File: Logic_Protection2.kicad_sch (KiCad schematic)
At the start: 10 parts

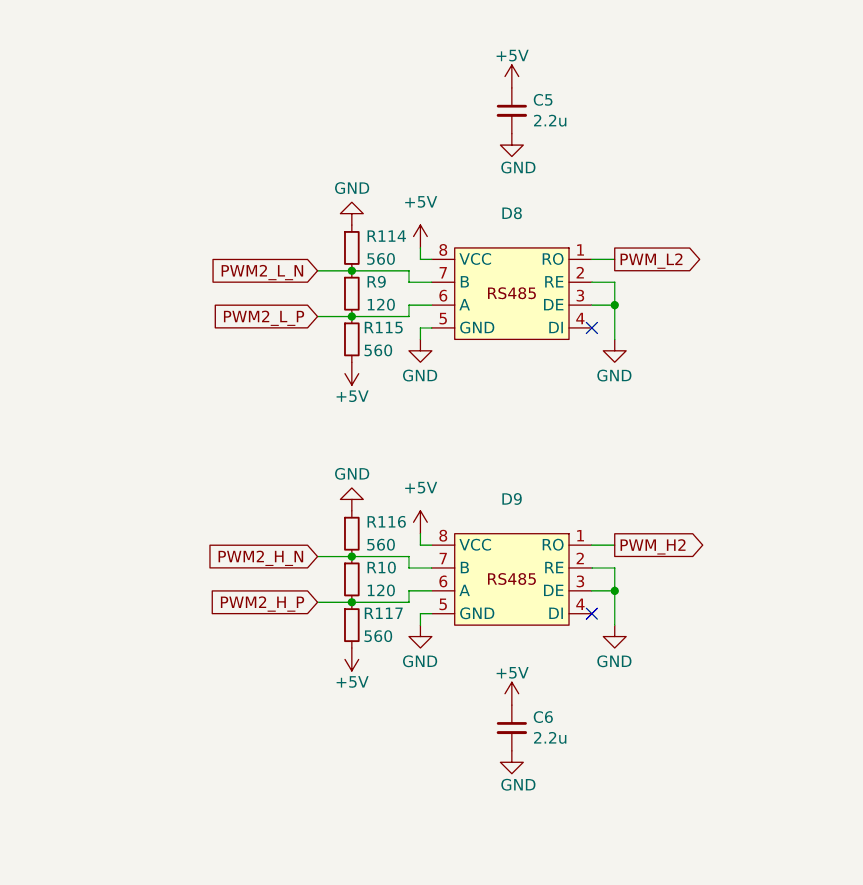
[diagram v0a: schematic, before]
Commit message: VER2.2: добавил фильтры на вход ШИМа и обновил все доки
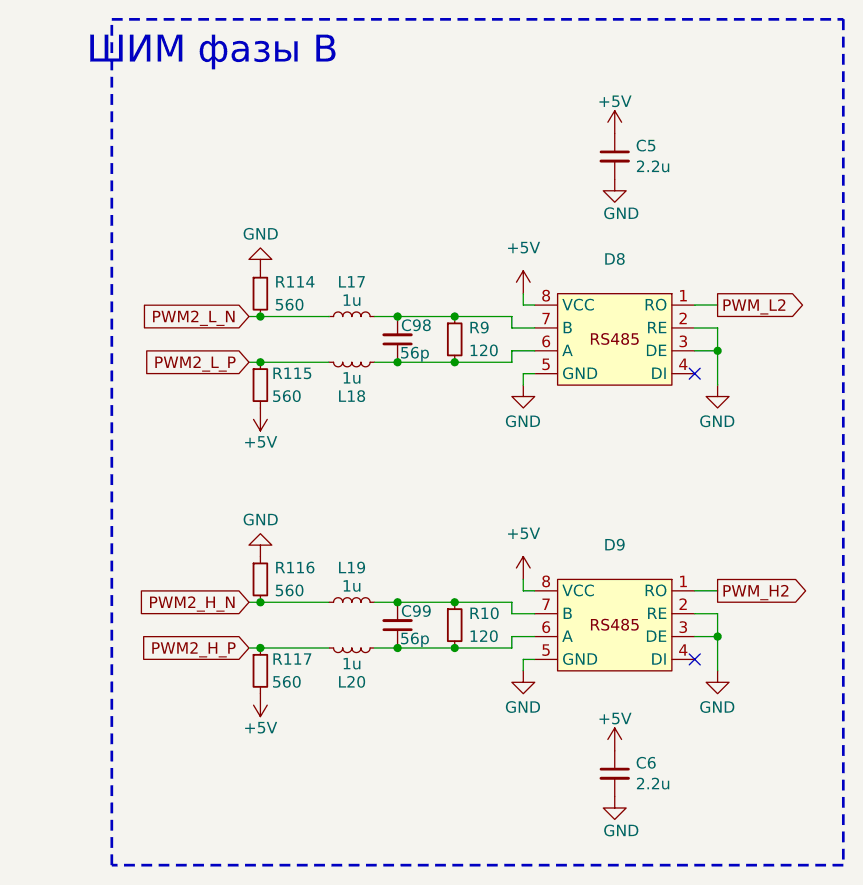
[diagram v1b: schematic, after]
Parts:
- added C98, C99: 56p, Capacitor_SMD:C_0805_2012Metric_Pad1.18x1.45mm_HandSolder, symbol Device:C_Small
- added L17, L18, L19, L20: 1u, Inductor_SMD:L_0603_1608Metric_Pad1.05x0.95mm_HandSolder, symbol Device:L_Small
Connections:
- net PWM2_H_N: now also L19.1; no longer D9.7 (B), R10.1
- net PWM2_H_P: now also L20.2; no longer D9.6 (A), R10.2
- net PWM2_L_N: now also L17.1; no longer D8.7 (B), R9.1
- net PWM2_L_P: now also L18.2; no longer D8.6 (A), R9.2
- new net: C98.1, D8.6 (A), L18.1, R9.2
- new net: C98.2, D8.7 (B), L17.2, R9.1
- new net: C99.1, D9.6 (A), L20.1, R10.2
- new net: C99.2, D9.7 (B), L19.2, R10.1
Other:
- note added: "ШИМ фазы B"
- company: (none) -> ООО "ЭТТ"
- moved on the sheet: C5, C6, D8, D9, R10, R114, R115, R116, R117, R9

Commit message: VER2.2.1: создал папку для производственных доков
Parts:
- C5, C6, C98, C99: Description P/N (none) -> Capacitor SMD 25+V
- R10, R114, R115, R116, R117, R9: Description P/N (none) -> Resistor SMD
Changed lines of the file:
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@@
 			)
 		)
-		(property "Description P/N" ""
+		(property "Description P/N" "Capacitor SMD 25+V"
 			(at 140.97 86.36 0)
 			(effects
@@
 			)
 		)
-		(property "Description P/N" ""
+		(property "Description P/N" "Capacitor SMD 25+V"
 			(at 140.97 118.11 0)
 			(effects
@@
 			)
 		)
-		(property "Description P/N" ""
+		(property "Description P/N" "Resistor SMD"
 			(at 125.73 123.19 0)
 			(effects
@@
 			)
 		)
-		(property "Description P/N" ""
+		(property "Description P/N" "Resistor SMD"
 			(at 147.32 86.36 0)
 			(effects
@@
 			)
 		)
-		(property "Description P/N" ""
+		(property "Description P/N" "Capacitor SMD 25+V"
 			(at 165.1 134.62 0)
 			(effects
@@
 			)
 		)
-		(property "Description P/N" ""
+		(property "Description P/N" "Resistor SMD"
 			(at 125.73 91.44 0)
 			(effects
@@
 			)
 		)
-		(property "Description P/N" ""
+		(property "Description P/N" "Resistor SMD"
 			(at 125.73 81.28 0)
 			(effects
@@
 			)
 		)
-		(property "Description P/N" ""
+		(property "Description P/N" "Capacitor SMD 25+V"
 			(at 165.1 66.04 0)
 			(effects
@@
 			)
 		)
-		(property "Description P/N" ""
+		(property "Description P/N" "Resistor SMD"
 			(at 125.73 113.03 0)
 			(effects
@@
 			)
 		)
-		(property "Description P/N" ""
+		(property "Description P/N" "Resistor SMD"
 			(at 147.32 118.11 0)
 			(effects
